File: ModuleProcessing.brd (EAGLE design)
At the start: 52 x 42.9 mm, 24 parts, among them IC1 INA128U, IC2 LM358MX, IC3 MCP606-I_SN

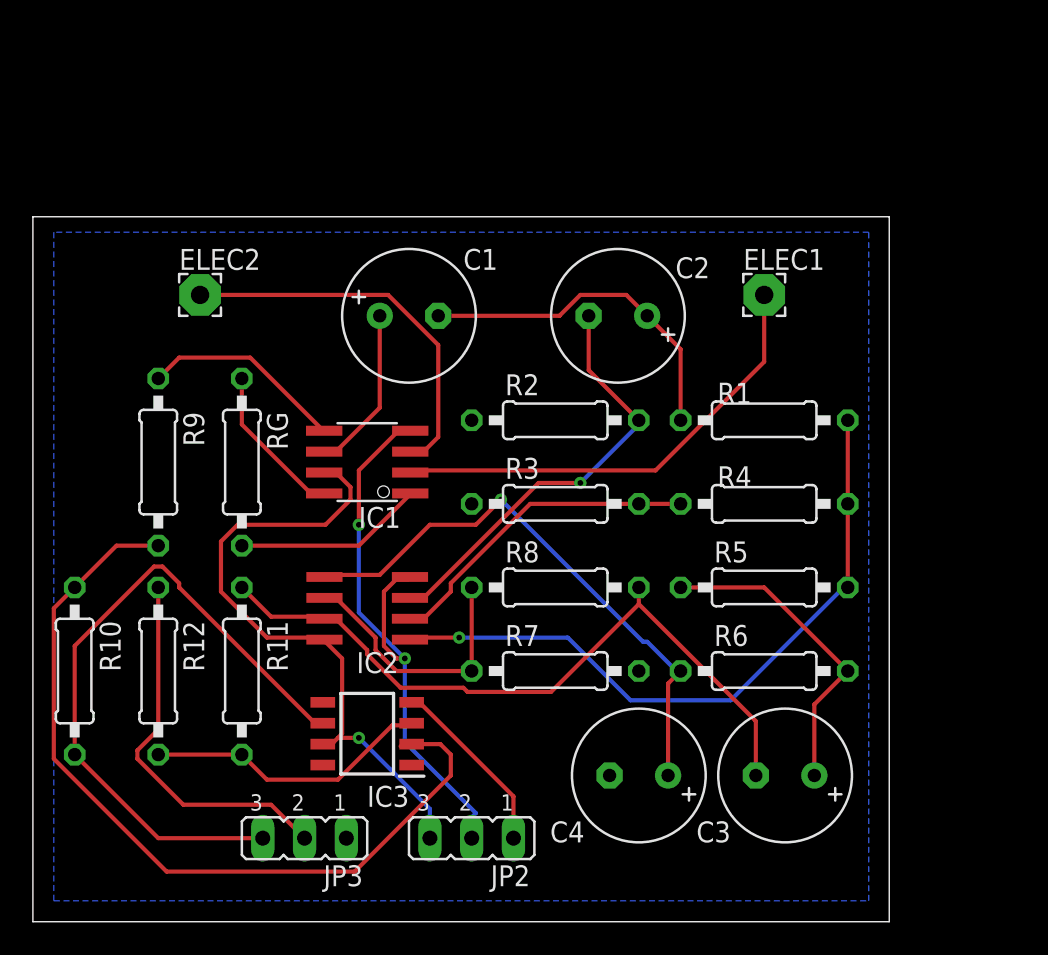
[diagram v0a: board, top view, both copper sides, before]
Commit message: Added bypass capacitors on Processing Module
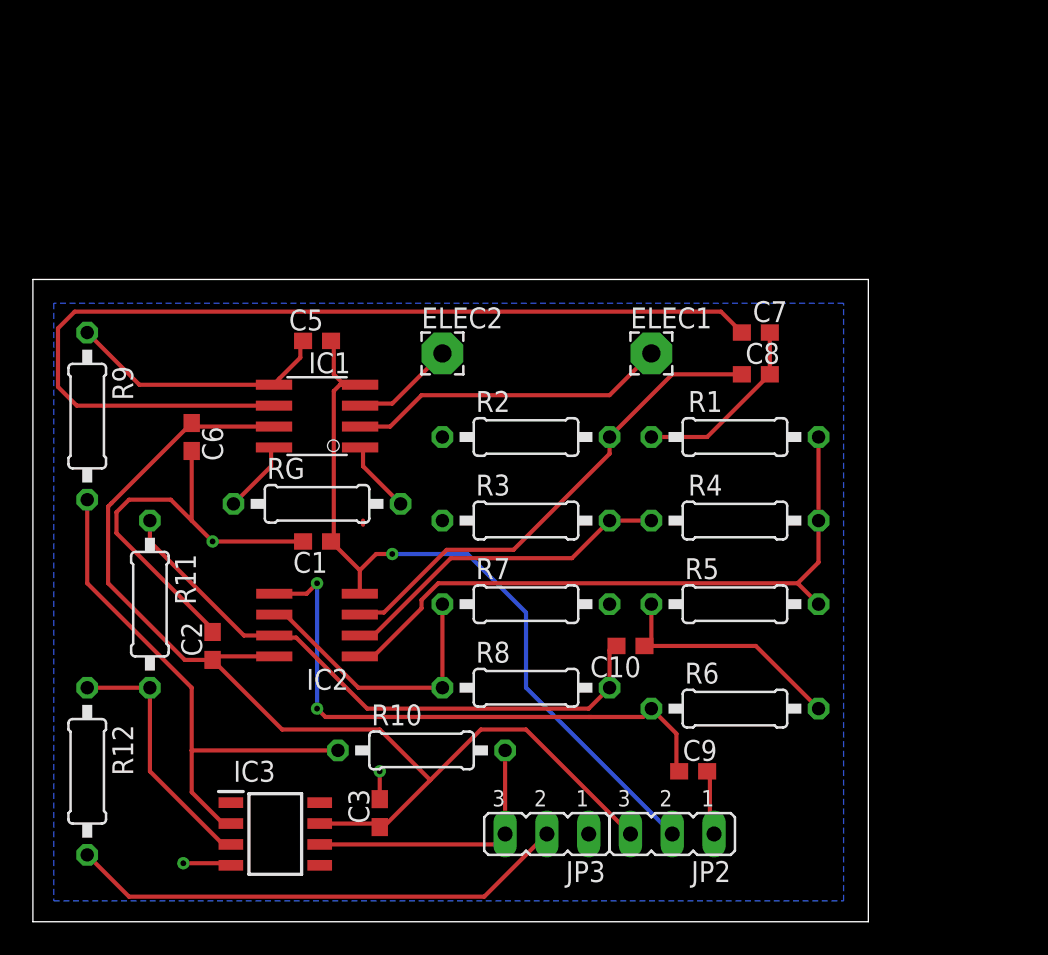
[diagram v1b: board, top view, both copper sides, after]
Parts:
- removed C4: (no value), rcl:E3,5-8
- added C10, C5, C6, C7, C8, C9: (no value), rcl:C0603
- C1, C2, C3: device rcl:E3,5-8 -> rcl:C0603
- moved C2 31.8 mm to (10.9, 16.8), turned to 90 degrees
- moved C3 24.7 mm to (21.1, 6.60), turned to 90 degrees
- moved R10 21.6 mm to (23.6, 10.4), turned to 0 degrees
- moved ELEC2 15.2 mm to (24.9, 34.5)
- moved C1 14.8 mm to (17.3, 23.1), turned to 180 degrees
- moved JP3 14.7 mm to (31.2, 5.33)
- moved JP2 12.2 mm to (38.9, 5.33)
- moved IC3 8.27 mm to (14.7, 5.33), turned to 0 degrees
- moved ELEC1 7.73 mm to (37.6, 34.5)
- moved R12 7.47 mm to (3.30, 9.14), turned to 90 degrees
- moved R11 6.91 mm to (7.11, 19.3)
- moved R8 6.35 mm to (30.0, 14.2)
- moved RG 5.23 mm to (17.3, 25.4), turned to 0 degrees
- moved R9 5.14 mm to (3.30, 30.7)
- moved R7 4.44 mm to (30.0, 19.3)
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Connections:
- net AGND: now also C1.2, C2.2, C3.2, C5.2, C6.2, C9.2; no longer C4.-
- net N$10: now also C10.2; no longer C3.-
- net N$5: now also C8.1; no longer C2.-
- net N$6: now also C7.1, C8.2; no longer C1.-, C2.+
- net N$7: now also C7.2; no longer C1.+
- net N$8: now also C10.1; no longer C3.+
- net N$9: now also C9.1; no longer C4.+
- net VDD: now also C2.1, C3.1, C6.1
- net VSS: now also C1.1, C5.1
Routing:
- net N$7: track 10.1 -> 59.8 mm
- net VDD: track 38.9 -> 69.6 mm, vias 1 -> 0
- net AGND: track 23.5 -> 51.9 mm, vias 0 -> 3
- net SIGOUT: track 41.3 -> 16.6 mm
- net N$13: track 51.1 -> 32.5 mm
- net ELEC2: track 23.4 -> 6.31 mm
- net VSS: track 36.4 -> 49.5 mm, vias 2 -> 1
- net N$6: track 20.9 -> 11.3 mm
- net ELEC1: track 28.4 -> 19.8 mm
- net VREF: track 23.1 -> 30.6 mm
- net N$1: track 11.6 -> 4.47 mm
- net N$10: track 43.5 -> 37.0 mm
- net N$2: track 9.52 -> 4.47 mm
- net N$8: track 19.5 -> 14.7 mm
- net N$5: track 26.1 -> 29.9 mm, vias 1 -> 0
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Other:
- board size 52 x 42.9 mm -> 50.8 x 39 mm

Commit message: Changed board for testing before final prototype
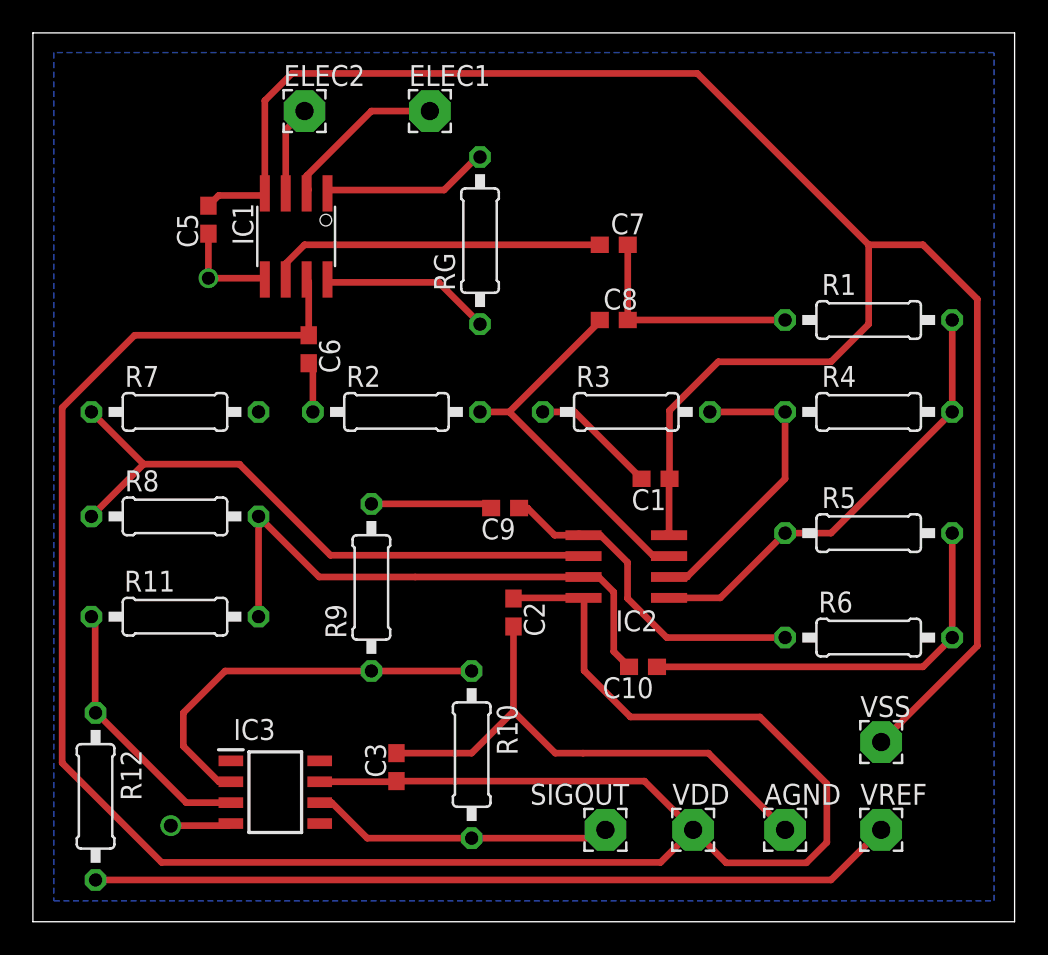
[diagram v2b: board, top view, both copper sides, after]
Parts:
- removed JP2, JP3: (no value), jumper:JP2
- added AGND, SIGOUT, VDD, VREF, VSS: WIREPAD2,54/1,1, wirepad:2,54/1,1
- moved R7 24.3 mm to (8.64, 31.0)
- moved R8 23.7 mm to (8.64, 24.6)
- moved C1 20.9 mm to (37.8, 26.9)
- moved R9 20.2 mm to (20.6, 20.3)
- moved ELEC1 20.0 mm to (24.1, 49.3)
- moved C9 19.7 mm to (28.7, 25.1), turned to 180 degrees
- moved IC2 19.1 mm to (36.1, 21.6)
- moved RG 18.8 mm to (27.2, 41.4), turned to 90 degrees
- moved C2 18.4 mm to (29.2, 18.8), turned to 270 degrees
- moved ELEC2 16.9 mm to (16.5, 49.3)
- moved IC1 11.0 mm to (16.0, 41.7), turned to 180 degrees
- moved R1 10.8 mm to (50.8, 36.6)
- moved R4 10.5 mm to (50.8, 31.0)
- moved C7 10.2 mm to (35.3, 41.1)
- moved C5 9.89 mm to (10.7, 42.7), turned to 270 degrees
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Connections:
- removed net N$19: JP3.1
- net AGND: now also AGND.1; no longer JP2.1
- net SIGOUT: now also SIGOUT.1; no longer JP3.3
- net VDD: now also VDD.1; no longer JP2.3
- net VREF: now also VREF.1; no longer JP3.2
- net VSS: now also VSS.1; no longer JP2.2
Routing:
- net VDD: track 69.6 -> 147.2 mm
- net VSS: track 49.5 -> 115.6 mm, vias 1 -> 0
- net N$7: track 59.8 -> 21.4 mm
- net N$11: track 17.3 -> 38.0 mm
- net VREF: track 30.6 -> 49.0 mm
- net N$9: track 36.4 -> 21.4 mm, vias 2 -> 0
- net N$4: track 39.9 -> 27.5 mm
- net N$8: track 14.7 -> 25.0 mm
- net AGND: track 51.9 -> 61.8 mm, vias 3 -> 2
- net ELEC1: track 19.8 -> 10.5 mm
- net N$13: track 32.5 -> 24.4 mm
- net N$5: track 29.9 -> 23.2 mm
- net N$2: track 4.47 -> 10.4 mm
- net N$1: track 4.47 -> 10.2 mm
- net N$6: track 11.3 -> 14.1 mm
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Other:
- board size 50.8 x 39 mm -> 59.7 x 54 mm

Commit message: Final version of processing pre-prototype
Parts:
- removed C10: (no value), rcl:C0603
- removed R1: (no value), rcl:0207/10
- added C4: (no value), rcl:C0603
- added R13: (no value), rcl:0207/10
- moved R7 44.3 mm to (50.8, 17.3)
- moved C3 34.4 mm to (35.3, 41.1), turned to 180 degrees
- moved C1 31.4 mm to (10.7, 42.7), turned to 270 degrees
- moved C5 30.2 mm to (29.2, 18.8)
- moved C6 22.5 mm to (37.8, 26.9), turned to 180 degrees
- moved C8 21.2 mm to (37.1, 15.5), turned to 180 degrees
- moved C2 20.3 mm to (16.8, 34.8)
- moved R10 19.9 mm to (8.64, 18.5), turned to 180 degrees
- moved C7 17.3 mm to (28.7, 25.1)
- moved C9 17.1 mm to (22.1, 9.40), turned to 90 degrees
- moved R3 15.8 mm to (50.8, 36.6), turned to 180 degrees
- moved R4 14.7 mm to (36.1, 31.0), turned to 0 degrees
- moved R9 12.7 mm to (8.64, 24.6), turned to 0 degrees
- moved R11 12.1 mm to (20.6, 20.3), turned to 270 degrees
- moved R5 7.37 mm to (50.8, 31.0)
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- renumbered AGND to PAD5, ELEC1 to PAD1, ELEC2 to PAD2, SIGOUT to PAD6, VDD to PAD3, VREF to PAD7, VSS to PAD4
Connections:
- net AGND: now also C7.2, R11.1, R4.1, R8.2; no longer C3.2, R3.1, R7.2, R9.1
- net N$10: now also C8.2, R10.1, R9.2; no longer C10.2, R11.1, R8.2
- net N$11: now also R9.1; no longer R7.1
- net N$12: now also R10.2; no longer R11.2
- net N$13: now also R11.2, R13.1; no longer R10.1, R9.2
- net N$3: now also R5.2; no longer R3.2
- net N$4: now also R3.1, R5.1, R6.2; no longer R1.1, R4.1, R5.2
- net N$5: now also C4.1; no longer C8.1
- net N$6: now also C3.1, C4.2, R3.2; no longer C7.1, C8.2, R1.2
- net N$7: now also C3.2; no longer C7.2
- net N$8: now also C8.1, R6.1, R7.2; no longer C10.1, R5.1, R6.2
- net N$9: now also C7.1, R7.1; no longer C9.1, R6.1
- net SIGOUT: now also R13.2; no longer R10.2
- net VDD: now also C5.1, C9.1; no longer C3.1, C6.1
- net VSS: now also C6.1; no longer C5.1
